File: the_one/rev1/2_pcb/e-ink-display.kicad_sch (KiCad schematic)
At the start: 1 part, among them J1 JST-PH 2.0mm

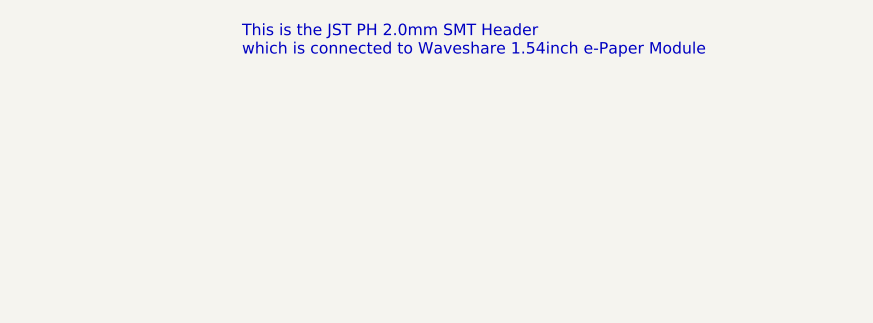
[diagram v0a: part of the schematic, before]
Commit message: update KiCad project references
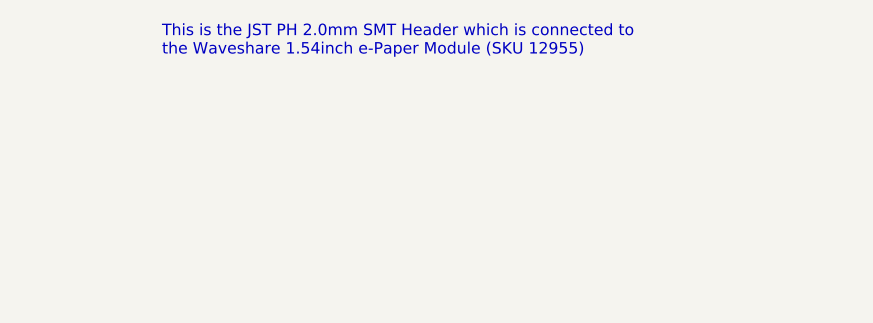
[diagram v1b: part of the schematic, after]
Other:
- note added: "This is the JST PH 2.0mm SMT Header which is connected to the Waveshare 1.54inch e-Paper Module (SKU 12955)"
- note removed: "This is the JST PH 2.0mm SMT Header which is connected to Waveshare 1.54inch e-Paper Module"
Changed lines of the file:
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@@
 		(company "tuantran39")
 	)
-	(text "This is the JST PH 2.0mm SMT Header\nwhich is connected to Waveshare 1.54inch e-Paper Module"
+	(text "This is the JST PH 2.0mm SMT Header which is connected to \nthe Waveshare 1.54inch e-Paper Module (SKU 12955)"
 		(exclude_from_sim no)
-		(at 118.11 36.83 0)
+		(at 109.22 36.83 0)
 		(effects
 			(font
@@
 			(table_cell "Pin"
 				(exclude_from_sim no)
-				(at 117.856 41.402 0)
+				(at 108.966 41.402 0)
 				(size 7.62 3.81)
 				(margins 0.9525 0.9525 0.9525 0.9525)
@@
 			(table_cell "Symbol"
 				(exclude_from_sim no)
-				(at 125.476 41.402 0)
+				(at 116.586 41.402 0)
 				(size 20.32 3.81)
 				(margins 0.9525 0.9525 0.9525 0.9525)
@@
 			(table_cell "Description"
 				(exclude_from_sim no)
-				(at 145.796 41.402 0)
+				(at 136.906 41.402 0)
 				(size 36.83 3.81)
 				(margins 0.9525 0.9525 0.9525 0.9525)
@@
 			(table_cell "1"
 				(exclude_from_sim no)
-				(at 117.856 45.212 0)
+				(at 108.966 45.212 0)
 				(size 7.62 3.81)
 				(margins 0.9525 0.9525 0.9525 0.9525)
@@
 			(table_cell "E-INK_VCC"
 				(exclude_from_sim no)
-				(at 125.476 45.212 0)
+				(at 116.586 45.212 0)
 				(size 20.32 3.81)
 				(margins 0.9525 0.9525 0.9525 0.9525)
@@
 			(table_cell "3.3V/5V"
 				(exclude_from_sim no)
-				(at 145.796 45.212 0)
+				(at 136.906 45.212 0)
 				(size 36.83 3.81)
 				(margins 0.9525 0.9525 0.9525 0.9525)
@@
 			(table_cell "2"
 				(exclude_from_sim no)
-				(at 117.856 49.022 0)
+				(at 108.966 49.022 0)
 				(size 7.62 3.81)
 				(margins 0.9525 0.9525 0.9525 0.9525)
@@
 			(table_cell "GND"
 				(exclude_from_sim no)
-				(at 125.476 49.022 0)
+				(at 116.586 49.022 0)
 				(size 20.32 3.81)
 				(margins 0.9525 0.9525 0.9525 0.9525)
@@
 			(table_cell "Ground"
 				(exclude_from_sim no)
-				(at 145.796 49.022 0)
+				(at 136.906 49.022 0)
 				(size 36.83 3.81)
 				(margins 0.9525 0.9525 0.9525 0.9525)
@@
 			(table_cell "3"
 				(exclude_from_sim no)
-				(at 117.856 52.832 0)
+				(at 108.966 52.832 0)
 				(size 7.62 3.81)
 				(margins 0.9525 0.9525 0.9525 0.9525)
@@
 			(table_cell "E-INK_MOSI"
 				(exclude_from_sim no)
-				(at 125.476 52.832 0)
+				(at 116.586 52.832 0)
 				(size 20.32 3.81)
 				(margins 0.9525 0.9525 0.9525 0.9525)
@@
 			(table_cell "SPI MOSI Pin"
 				(exclude_from_sim no)
-				(at 145.796 52.832 0)
+				(at 136.906 52.832 0)
 				(size 36.83 3.81)
 				(margins 0.9525 0.9525 0.9525 0.9525)
@@
 			(table_cell "4"
 				(exclude_from_sim no)
-				(at 117.856 56.642 0)
+				(at 108.966 56.642 0)
 				(size 7.62 3.81)
 				(margins 0.9525 0.9525 0.9525 0.9525)
@@
 			(table_cell "E-INK_SCK"
 				(exclude_from_sim no)
-				(at 125.476 56.642 0)
+				(at 116.586 56.642 0)
 				(size 20.32 3.81)
 				(margins 0.9525 0.9525 0.9525 0.9525)
@@
 			(table_cell "SPI SCK Pin"
 				(exclude_from_sim no)
-				(at 145.796 56.642 0)
+				(at 136.906 56.642 0)
 				(size 36.83 3.81)
 				(margins 0.9525 0.9525 0.9525 0.9525)
@@
 			(table_cell "5"
 				(exclude_from_sim no)
-				(at 117.856 60.452 0)
+				(at 108.966 60.452 0)
 				(size 7.62 3.81)
 				(margins 0.9525 0.9525 0.9525 0.9525)
@@
 			(table_cell "E-INK_CS"
 				(exclude_from_sim no)
-				(at 125.476 60.452 0)
+				(at 116.586 60.452 0)
 				(size 20.32 3.81)
 				(margins 0.9525 0.9525 0.9525 0.9525)
@@
 			(table_cell "SPI Chip Selection, low active"
 				(exclude_from_sim no)
-				(at 145.796 60.452 0)
+				(at 136.906 60.452 0)
 				(size 36.83 3.81)
 				(margins 0.9525 0.9525 0.9525 0.9525)
@@
 			(table_cell "6"
 				(exclude_from_sim no)
-				(at 117.856 64.262 0)
+				(at 108.966 64.262 0)
 				(size 7.62 6.35)
 				(margins 0.9525 0.9525 0.9525 0.9525)
@@
 			(table_cell "E-INK_DC"
 				(exclude_from_sim no)
-				(at 125.476 64.262 0)
+				(at 116.586 64.262 0)
 				(size 20.32 6.35)
 				(margins 0.9525 0.9525 0.9525 0.9525)
@@
 			(table_cell "Data/Command (high for data, low for command)"
 				(exclude_from_sim no)
-				(at 145.796 64.262 0)
+				(at 136.906 64.262 0)
 				(size 36.83 6.35)
 				(margins 0.9525 0.9525 0.9525 0.9525)
@@
 			(table_cell "7"
 				(exclude_from_sim no)
-				(at 117.856 70.612 0)
+				(at 108.966 70.612 0)
 				(size 7.62 3.81)
 				(margins 0.9525 0.9525 0.9525 0.9525)
@@
 			(table_cell "E-INK_RST"
 				(exclude_from_sim no)
-				(at 125.476 70.612 0)
+				(at 116.586 70.612 0)
 				(size 20.32 3.81)
 				(margins 0.9525 0.9525 0.9525 0.9525)
@@
 			(table_cell "External reset, low active"
 				(exclude_from_sim no)
-				(at 145.796 70.612 0)
+				(at 136.906 70.612 0)
 				(size 36.83 3.81)
 				(margins 0.9525 0.9525 0.9525 0.9525)
@@
 			(table_cell "8"
 				(exclude_from_sim no)
-				(at 117.856 74.422 0)
+				(at 108.966 74.422 0)
 				(size 7.62 3.81)
 				(margins 0.9525 0.9525 0.9525 0.9525)
@@
 			(table_cell "E-INK_BUSY"
 				(exclude_from_sim no)
-				(at 125.476 74.422 0)
+				(at 116.586 74.422 0)
 				(size 20.32 3.81)
 				(margins 0.9525 0.9525 0.9525 0.9525)
@@
 			(table_cell "Busy status output, high active"
 				(exclude_from_sim no)
-				(at 145.796 74.422 0)
-				(size 36.83 3.81)
-				(margins 0.9525 0.9525 0.9525 0.9525)
+				(at 136.906 74.422 0)
+				(size 36.83 3.81)
+				(margins 0.9525 0.9525 0.9525 0.9525)

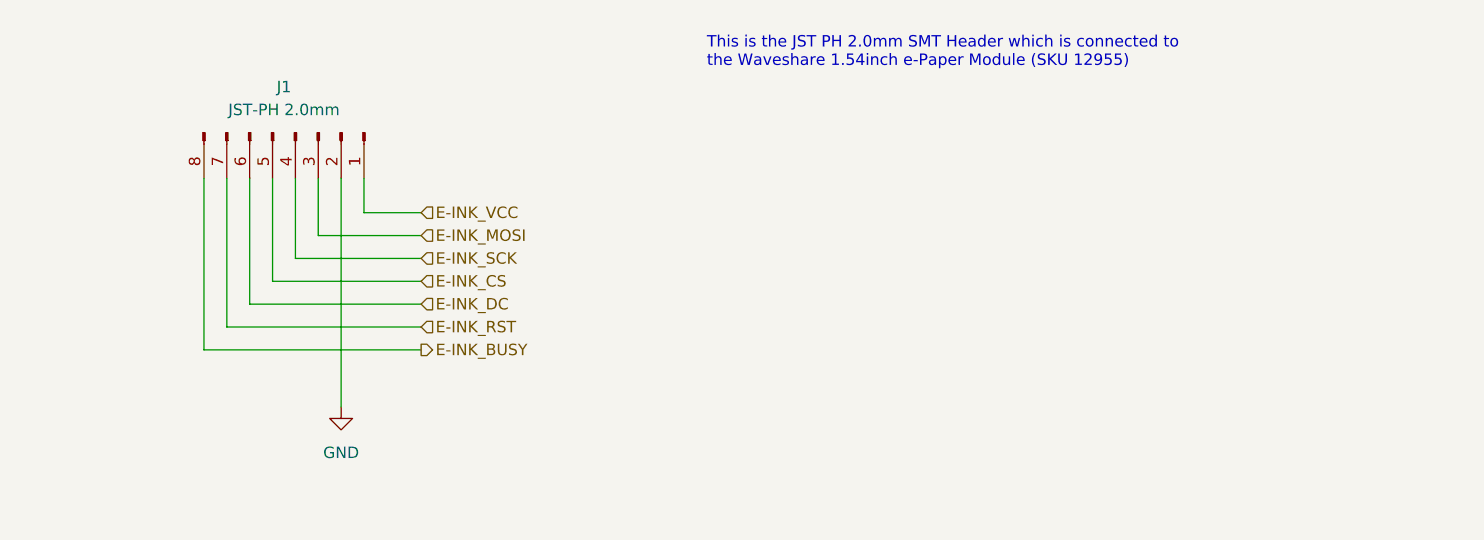
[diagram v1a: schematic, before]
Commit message: add capacitors near e-Ink Vcc pin
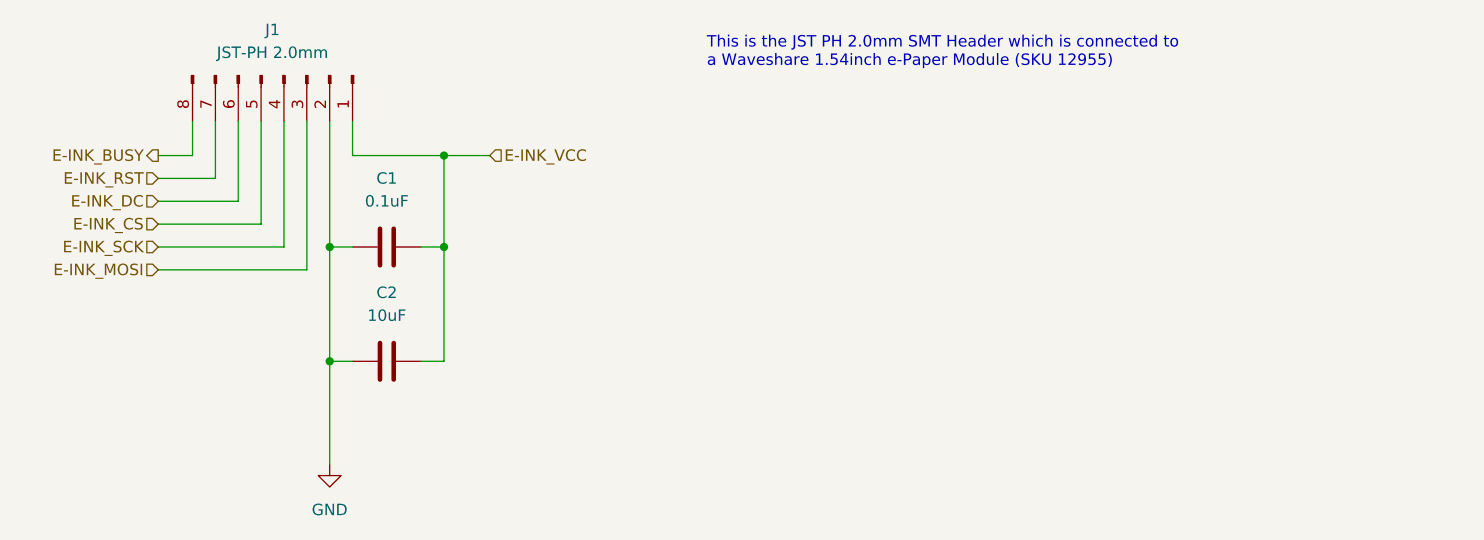
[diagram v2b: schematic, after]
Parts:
- added C1: 0.1uF, symbol Device:C
- added C2: 10uF, symbol Device:C
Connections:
- net E-INK_VCC: now also C1.1, C2.1
- net GND: now also C1.2, C2.2
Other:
- note added: "This is the JST PH 2.0mm SMT Header which is connected to a Waveshare 1.54inch e-Paper Module (SKU 12955)"
- note removed: "This is the JST PH 2.0mm SMT Header which is connected to the Waveshare 1.54inch e-Paper Module (SKU 12955)"
- moved on the sheet: J1

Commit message: update rev1 README
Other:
- moved on the sheet: C1, C2, J1
